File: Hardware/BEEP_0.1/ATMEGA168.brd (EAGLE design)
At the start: 48.8 x 53 mm, 23 parts, among them IC1 ATMEGA48/88/168-AU, Q1 20Mhz

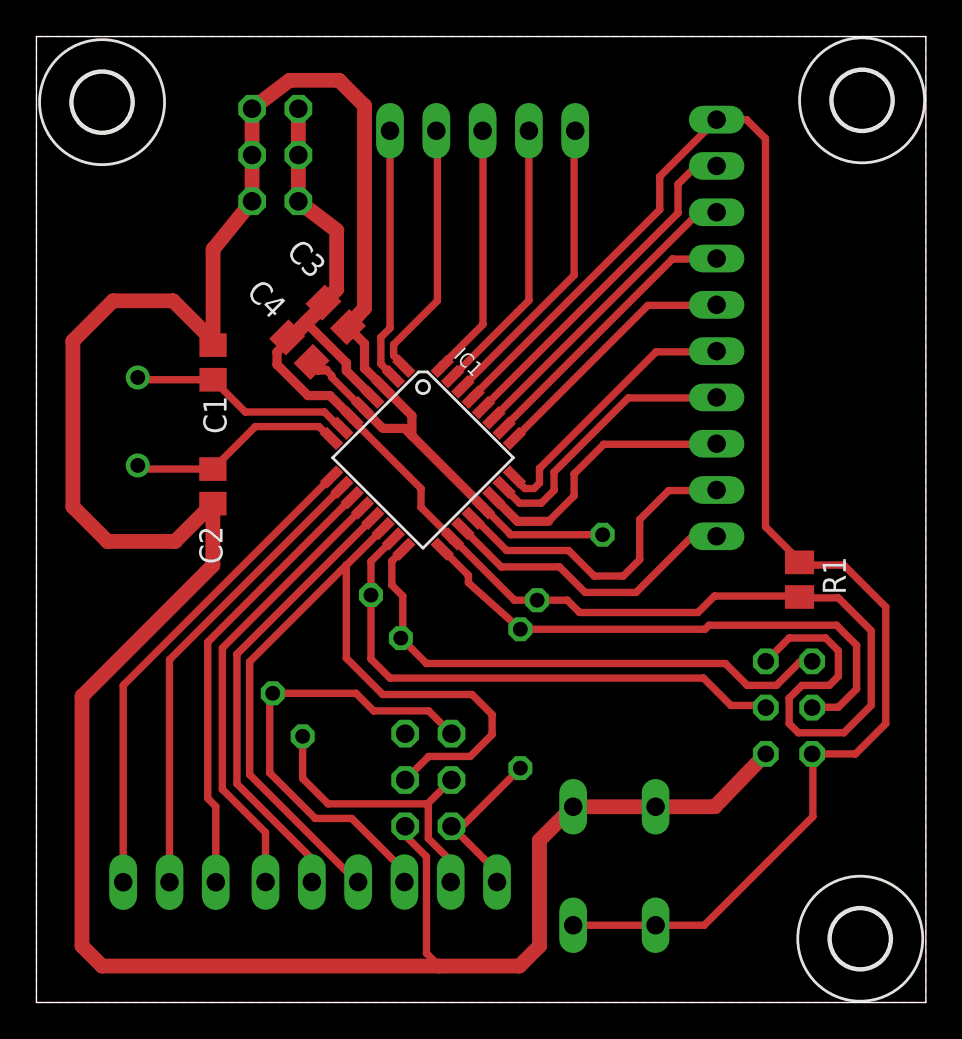
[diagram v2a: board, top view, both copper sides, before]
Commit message: rotate reset button on atmega board remove GND under TCS3103
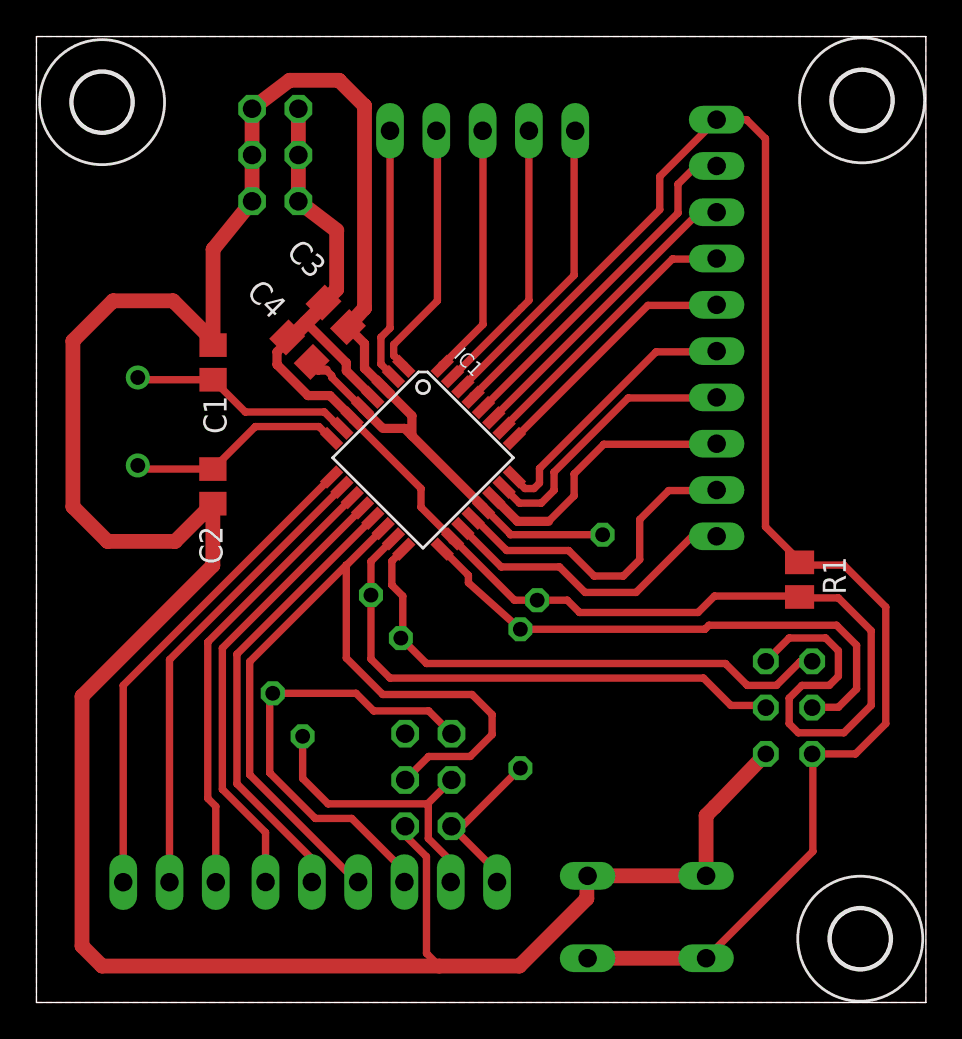
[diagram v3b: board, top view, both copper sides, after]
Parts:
- moved S1 3.32 mm to (33.5, 4.69), turned to 180 degrees
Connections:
- net GND: now also S1.3; no longer S1.2
- net RST: now also S1.2; no longer S1.3
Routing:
- net RST: track 83.8 -> 84.9 mm
- net GND: track 170.9 -> 170.2 mm
- added copper zone on layer 1, net N$19
- removed copper zone on layer 1, net GND
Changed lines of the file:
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@@
 <text x="45.9" y="27.2" size="1.778" layer="26" rot="MR0">AREF</text>
 <text x="46" y="24.8" size="1.778" layer="26" rot="MR0">ADC6</text>
-<text x="36.5" y="0.7" size="1.778" layer="26" rot="MR0">RESET</text>
+<text x="36.1" y="8.3" size="1.778" layer="26" rot="MR0">RESET</text>
 <text x="26.3" y="5.1" size="1.778" layer="26" rot="MR270">PB5</text>
 <text x="23.6" y="5.1" size="1.778" layer="26" rot="MR270">PB4</text>
@@
 <attribute name="OC_FARNELL" value="unknown" x="46.37" y="-5.41" size="1.778" layer="28" rot="MR270" display="off"/>
 </element>
-<element name="S1" library="switch-omron" package="B3F-10XX" value="" x="31.71" y="7.49" rot="MR90">
-<attribute name="OC_NEWARK" value="36M3542" x="15.2" y="26.54" size="1.778" layer="28" rot="MR90" display="off"/>
-<attribute name="MPN" value="B3F-1000" x="15.2" y="26.54" size="1.778" layer="28" rot="MR90" display="off"/>
-<attribute name="MF" value="" x="15.2" y="26.54" size="1.778" layer="28" rot="MR90" display="off"/>
-<attribute name="OC_FARNELL" value="176432" x="15.2" y="26.54" size="1.778" layer="28" rot="MR90" display="off"/>
+<element name="S1" library="switch-omron" package="B3F-10XX" value="" x="33.49" y="4.69" rot="MR180">
+<attribute name="OC_NEWARK" value="36M3542" x="52.54" y="21.2" size="1.778" layer="28" rot="MR180" display="off"/>
+<attribute name="MPN" value="B3F-1000" x="52.54" y="21.2" size="1.778" layer="28" rot="MR180" display="off"/>
+<attribute name="MF" value="" x="52.54" y="21.2" size="1.778" layer="28" rot="MR180" display="off"/>
+<attribute name="OC_FARNELL" value="176432" x="52.54" y="21.2" size="1.778" layer="28" rot="MR180" display="off"/>
 </element>
 <element name="R2" library="rcl" package="0207/7" value="1k" x="15.66" y="19.66" smashed="yes" rot="MR315">
@@
 <contactref element="C3" pad="1"/>
 <contactref element="S1" pad="4"/>
-<contactref element="S1" pad="2"/>
 <contactref element="ISP" pad="6"/>
 <contactref element="SPI" pad="6"/>
@@
 <contactref element="POWER" pad="6"/>
 <contactref element="POWER" pad="4"/>
-<polygon width="0.4064" layer="1">
-<vertex x="0" y="53"/>
-<vertex x="48.8" y="53"/>
-<vertex x="48.8" y="0"/>
-<vertex x="0" y="0"/>
-</polygon>
 <wire x1="11.83" y1="43.96" x2="11.83" y2="46.5" width="0.8128" layer="1"/>
 <wire x1="11.83" y1="46.5" x2="11.83" y2="49.04" width="0.8128" layer="1"/>
 <wire x1="13.89" y1="50.6" x2="11.83" y2="49.04" width="0.8128" layer="1"/>
-<wire x1="29.4494" y1="10.7412" x2="33.9706" y2="10.7412" width="0.8128" layer="1"/>
-<wire x1="33.9706" y1="10.7412" x2="37.2212" y2="10.7412" width="0.8128" layer="1"/>
 <wire x1="37.2212" y1="10.7412" x2="40.02" y2="13.64" width="0.8128" layer="1"/>
 <wire x1="31.066053125" y1="25.66605" x2="26" y2="25.66605" width="0.4064" layer="1"/>
 <wire x1="26" y1="25.66605" x2="26" y2="25.7" width="0.4064" layer="1"/>
-<wire x1="29.4494" y1="10.7412" x2="29.4412" y2="10.7412" width="0.8128" layer="1"/>
 <wire x1="9.69" y1="36.07" x2="9.69" y2="41.32" width="0.8128" layer="1"/>
 <wire x1="9.69" y1="41.32" x2="11.83" y2="43.96" width="0.8128" layer="1"/>
@@
 <wire x1="9.68" y1="27.37" x2="9.68" y2="23.98" width="0.8128" layer="1"/>
 <wire x1="22.1" y1="2" x2="26.5" y2="2" width="0.8128" layer="1"/>
-<wire x1="26.5" y1="2" x2="27.6" y2="3.1" width="0.8128" layer="1"/>
-<wire x1="27.6" y1="3.1" x2="27.6" y2="8.9" width="0.8128" layer="1"/>
-<wire x1="27.6" y1="8.9" x2="29.4412" y2="10.7412" width="0.8128" layer="1"/>
 <wire x1="21.4" y1="2.7" x2="22.1" y2="2" width="0.4064" layer="1"/>
 <wire x1="22.1" y1="2" x2="3.6" y2="2" width="0.8128" layer="1"/>
@@
 <wire x1="16.2" y1="34.3" x2="16.2" y2="34.4" width="0.4064" layer="1"/>
 <wire x1="16.2" y1="34.4" x2="15.9" y2="34.7" width="0.4064" layer="1"/>
+<contactref element="S1" pad="3"/>
+<wire x1="26.5" y1="2" x2="30.2" y2="5.7" width="0.8128" layer="1"/>
+<wire x1="30.2" y1="5.7" x2="30.2" y2="6.9118" width="0.8128" layer="1"/>
+<wire x1="30.2" y1="6.9118" x2="30.2388" y2="6.9506" width="0.8128" layer="1"/>
+<wire x1="30.2388" y1="6.9506" x2="36.7412" y2="6.9506" width="0.8128" layer="1"/>
+<wire x1="36.7412" y1="6.9506" x2="36.7412" y2="10.2612" width="0.8128" layer="1"/>
+<wire x1="36.7412" y1="10.2612" x2="37.2212" y2="10.7412" width="0.8128" layer="1"/>
+<wire x1="19.1" y1="31.5" x2="19" y2="31.5" width="0" layer="19" extent="1-1"/>
 </signal>
 <signal name="VCC">
@@
 <wire x1="23.96248125" y1="33.20816875" x2="23.96248125" y2="33.26248125" width="0.508" layer="1"/>
 <wire x1="44.3" y1="24" x2="42.02" y2="24" width="0.4064" layer="1"/>
-<contactref element="S1" pad="3"/>
-<wire x1="36.6388" y1="4.2388" x2="33.9706" y2="4.2388" width="0.4064" layer="1"/>
-<wire x1="33.9706" y1="4.2388" x2="29.4494" y2="4.2388" width="0.4064" layer="1"/>
 <wire x1="42.02" y1="24" x2="41.87" y2="24.15" width="0.4064" layer="1"/>
-<wire x1="36.6388" y1="4.2388" x2="42.6" y2="10.2" width="0.4064" layer="1"/>
-<wire x1="42.6" y1="10.2" x2="42.6" y2="13.6" width="0.4064" layer="1"/>
+<wire x1="42.6" y1="8.2882" x2="42.6" y2="13.6" width="0.4064" layer="1"/>
 <wire x1="42.6" y1="13.6" x2="42.56" y2="13.64" width="0.4064" layer="1"/>
 <wire x1="42.56" y1="13.64" x2="44.94" y2="13.64" width="0.4064" layer="1"/>
@@
 <wire x1="34.2" y1="45.32" x2="37.32" y2="48.44" width="0.4064" layer="1"/>
 <wire x1="37.32" y1="48.44" x2="38.96" y2="48.44" width="0.4064" layer="1"/>
+<contactref element="S1" pad="2"/>
+<wire x1="30.2388" y1="2.4294" x2="36.7412" y2="2.4294" width="0.8128" layer="1"/>
+<wire x1="42.6" y1="8.2882" x2="36.7412" y2="2.4294" width="0.4064" layer="1"/>
 </signal>
 <signal name="MISO">
@@
 <wire x1="37.29" y1="33.17" x2="37.32" y2="33.2" width="0.4064" layer="1"/>
 </signal>
+<signal name="N$19">
+<polygon width="0.4064" layer="1">
+<vertex x="0" y="0"/>
+<vertex x="48.8" y="0"/>
+<vertex x="48.8" y="53"/>
+<vertex x="0" y="53"/>
+</polygon>
+</signal>
 </signals>
